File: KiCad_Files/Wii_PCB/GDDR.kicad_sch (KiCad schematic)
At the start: 2 parts

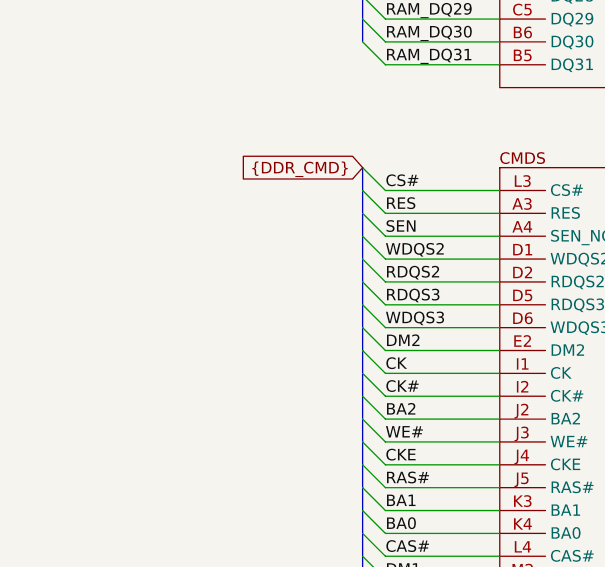
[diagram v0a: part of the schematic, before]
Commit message: Corrected C160 & RAM ZQ
C160 was updated from 4.7uF to 100nF.
RAM ZQ was grounded, it was working while floating, but updating anyway to ensure proper function.
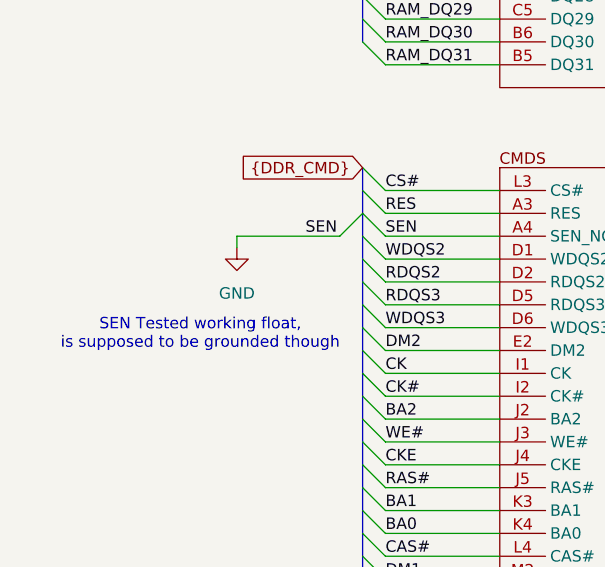
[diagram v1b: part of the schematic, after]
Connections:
- net SEN is gone; now on net GND: RAM1.A4 (SEN_NC)
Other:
- note added: "SEN Tested working float, is supposed to be grounded though"
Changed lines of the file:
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@@
 	(generator_version "9.0")
 	(paper "A4")
+	(text "SEN Tested working float,\nis supposed to be grounded though"
+		(exclude_from_sim no)
+		(at 27.686 145.542 0)
+		(effects
+			(font
+				(size 1.27 1.27)
+			)
+		)
+	)
 	(junction
 		(at 254 109.22)
@@
 	(bus_entry
 		(at 45.72 132.08)
+		(size -2.54 2.54)
+		(stroke
+			(width 0)
+			(type default)
+		)
+	)
+	(bus_entry
+		(at 45.72 132.08)
 		(size 2.54 2.54)
 		(stroke
@@
 	(wire
 		(pts
+			(xy 31.75 134.62) (xy 43.18 134.62)
+		)
+		(stroke
+			(width 0)
+			(type default)
+		)
+	)
+	(wire
+		(pts
 			(xy 254 116.84) (xy 243.84 116.84)
 		)
@@
 	(wire
 		(pts
+			(xy 31.75 134.62) (xy 31.75 135.89)
+		)
+		(stroke
+			(width 0)
+			(type default)
+		)
+	)
+	(wire
+		(pts
 			(xy 205.74 80.01) (xy 205.74 82.55)
 		)
@@
 		)
 	)
+	(label "SEN"
+		(at 39.37 134.62 0)
+		(effects
+			(font
+				(size 1.27 1.27)
+			)
+			(justify left bottom)
+		)
+	)
 	(label "RAM_A3"
 		(at 92.71 44.45 0)
@@
 	)
 	(symbol
-		(lib_name "Updated_GDDR3_1")
+		(lib_id "power:GND")
+		(at 31.75 135.89 0)
+		(unit 1)
+		(exclude_from_sim no)
+		(in_bom yes)
+		(on_board yes)
+		(dnp no)
+		(fields_autoplaced yes)
+		(property "Reference" "#PWR016"
+			(at 31.75 142.24 0)
+			(effects
+				(font
+					(size 1.27 1.27)
+				)
+				(hide yes)
+			)
+		)
+		(property "Value" "GND"
+			(at 31.75 140.97 0)
+			(effects
+				(font
+					(size 1.27 1.27)
+				)
+			)
+		)
+		(property "Footprint" ""
+			(at 31.75 135.89 0)
+			(effects
+				(font
+					(size 1.27 1.27)
+				)
+				(hide yes)
+			)
+		)
+		(property "Datasheet" ""
+			(at 31.75 135.89 0)
+			(effects
+				(font
+					(size 1.27 1.27)
+				)
+				(hide yes)
+			)
+		)
+		(property "Description" "Power symbol creates a global label with name \"GND\" , ground"
+			(at 31.75 135.89 0)
+			(effects
+				(font
+					(size 1.27 1.27)
+				)
+				(hide yes)
+			)
+		)
+		(pin "1"
+		)
+		(instances
+			(project "Wii PCB"
+				(path "/07becb85-5b32-497c-802d-66c73e9db46a/2c30263e-9c9a-4ac3-91af-18e443e3dbbc"
+					(reference "#PWR016")
+					(unit 1)
+				)
+			)
+		)
+	)
+	(symbol
 		(lib_id "Wii_symbols:Updated_GDDR3")
 		(at 74.93 29.21 0)

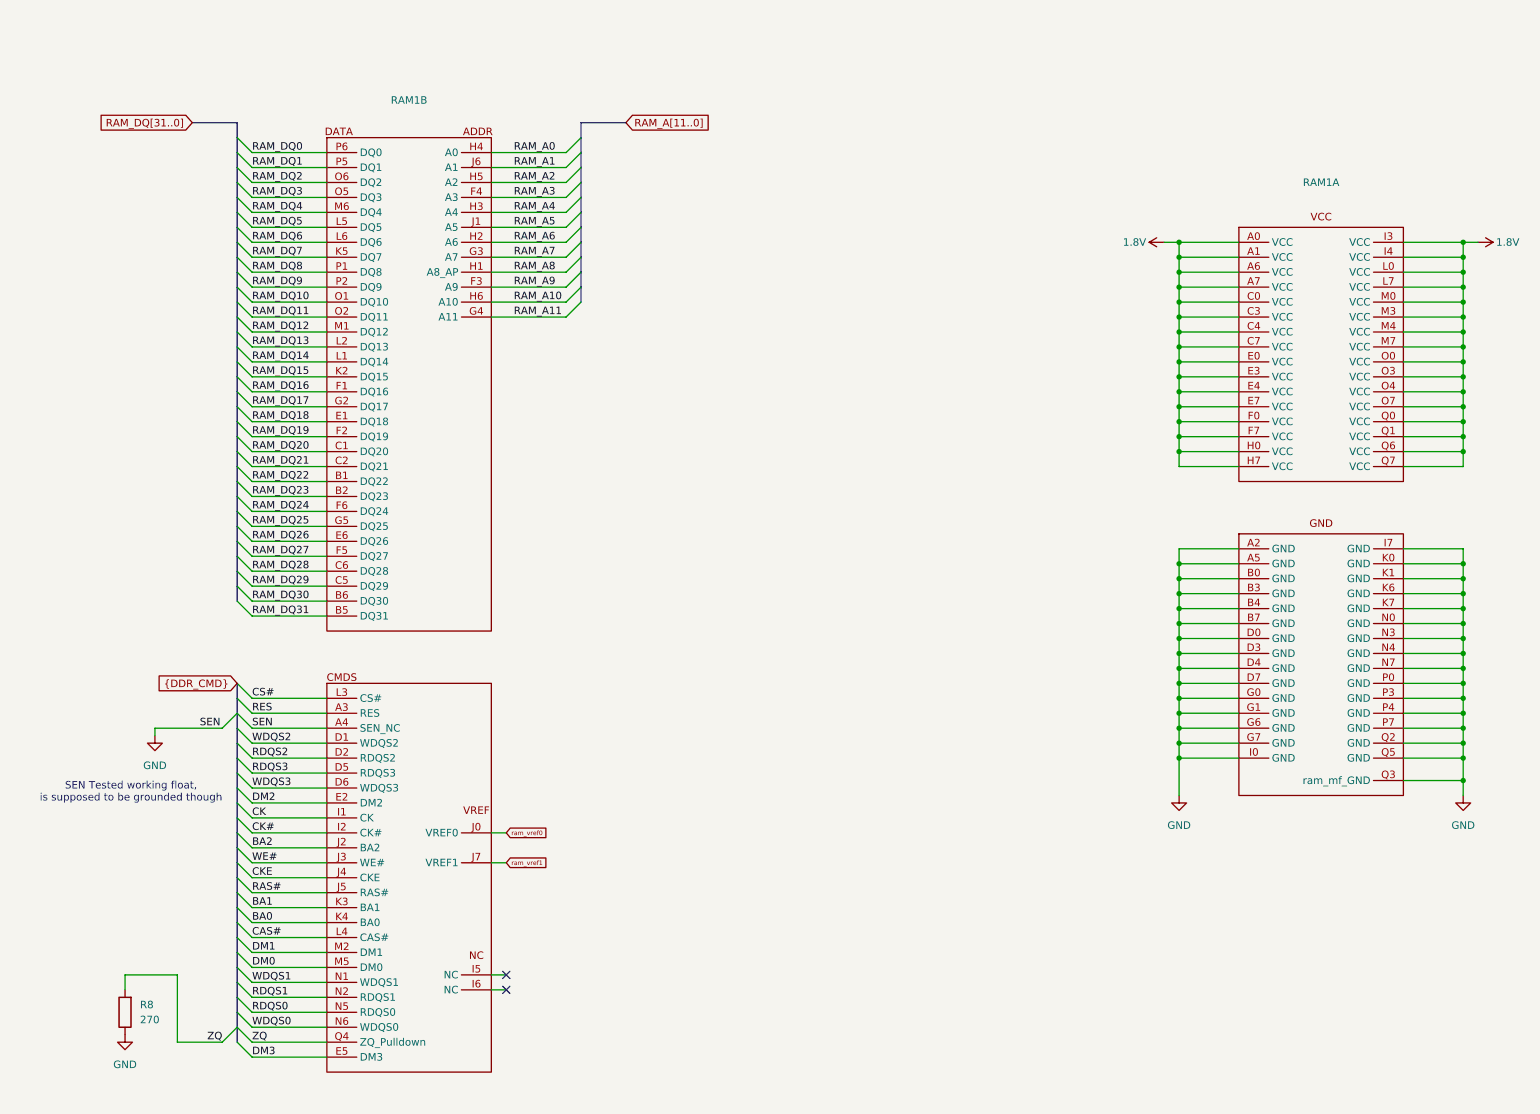
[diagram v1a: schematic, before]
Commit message: Updated RAM & GPU bus to allow custom net rules for measuring intra-track spacing, added pad for reset, removed debug pads, reorganized ram schematic to cluster length matched signals, changed MX chip and U10 symbols, and re-labeled the wifi net interface.
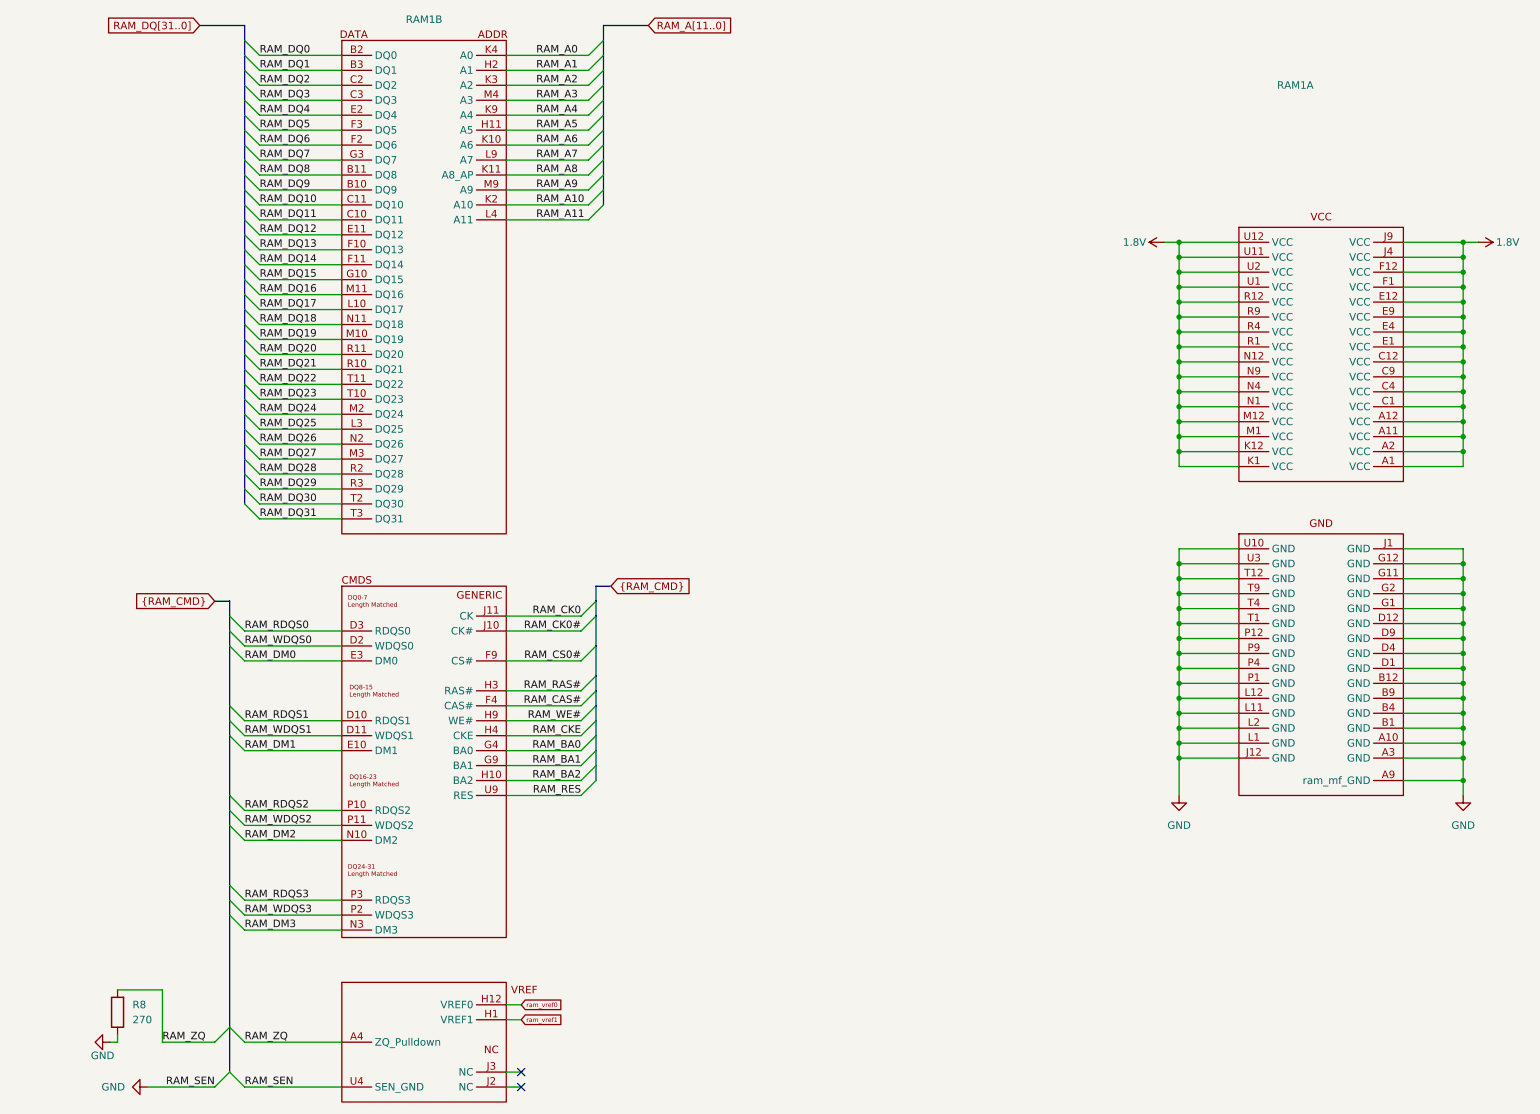
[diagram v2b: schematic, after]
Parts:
- removed RAM1: ~, wii_bgaLibrary:GDDR3, symbol Wii_symbols:Updated_GDDR3
- added RAM1: ~, WeeWii_Library:Updated GDDR3, symbol Wii_symbols:New_Updated_GDDR3
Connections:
- net 1.8V: now also RAM1.A1 (VCC), RAM1.A11 (VCC), RAM1.A12 (VCC), RAM1.A2 (VCC), RAM1.C1 (VCC), RAM1.C12 (VCC), RAM1.C4 (VCC), RAM1.C9 (VCC), RAM1.E1 (VCC), RAM1.E12 (VCC), RAM1.E4 (VCC), RAM1.E9 (VCC), RAM1.F1 (VCC), RAM1.F12 (VCC), RAM1.J4 (VCC), RAM1.J9 (VCC), RAM1.K1 (VCC), RAM1.K12 (VCC), RAM1.M1 (VCC), RAM1.M12 (VCC), RAM1.N1 (VCC), RAM1.N12 (VCC), RAM1.N4 (VCC), RAM1.N9 (VCC), RAM1.R1 (VCC), RAM1.R12 (VCC), RAM1.R4 (VCC), RAM1.R9 (VCC), RAM1.U1 (VCC), RAM1.U11 (VCC), RAM1.U12 (VCC), RAM1.U2 (VCC)
- net GND: now also RAM1.A10 (GND), RAM1.A3 (GND), RAM1.A9 (ram_mf_GND), RAM1.B1 (GND), RAM1.B12 (GND), RAM1.B4 (GND), RAM1.B9 (GND), RAM1.D1 (GND), RAM1.D12 (GND), RAM1.D4 (GND), RAM1.D9 (GND), RAM1.G1 (GND), RAM1.G11 (GND), RAM1.G12 (GND), RAM1.G2 (GND), RAM1.J1 (GND), RAM1.J12 (GND), RAM1.L1 (GND), RAM1.L11 (GND), RAM1.L12 (GND), RAM1.L2 (GND), RAM1.P1 (GND), RAM1.P12 (GND), RAM1.P4 (GND), RAM1.P9 (GND), RAM1.T1 (GND), RAM1.T12 (GND), RAM1.T4 (GND), RAM1.T9 (GND), RAM1.U10 (GND), RAM1.U3 (GND), RAM1.U4 (SEN_GND)
- net RAM_A0: now also RAM1.K4 (A0)
- net RAM_A1: now also RAM1.H2 (A1)
- net RAM_A10: now also RAM1.K2 (A10)
- net RAM_A11: now also RAM1.L4 (A11)
- net RAM_A2: now also RAM1.K3 (A2)
- net RAM_A3: now also RAM1.M4 (A3)
- net RAM_A4: now also RAM1.K9 (A4)
- net RAM_A5: now also RAM1.H11 (A5)
- net RAM_A6: now also RAM1.K10 (A6)
- net RAM_A7: now also RAM1.L9 (A7)
- net RAM_A8: now also RAM1.K11 (A8_AP)
- net RAM_A9: now also RAM1.M9 (A9)
- net RAM_DQ0: now also RAM1.B2 (DQ0)
- net RAM_DQ1: now also RAM1.B3 (DQ1)
- net RAM_DQ10: now also RAM1.C11 (DQ10)
- net RAM_DQ11: now also RAM1.C10 (DQ11)
- net RAM_DQ12: now also RAM1.E11 (DQ12)
- net RAM_DQ13: now also RAM1.F10 (DQ13)
- net RAM_DQ14: now also RAM1.F11 (DQ14)
- net RAM_DQ15: now also RAM1.G10 (DQ15)
- net RAM_DQ16: now also RAM1.M11 (DQ16)
- net RAM_DQ17: now also RAM1.L10 (DQ17)
- net RAM_DQ18: now also RAM1.N11 (DQ18)
- net RAM_DQ19: now also RAM1.M10 (DQ19)
- net RAM_DQ2: now also RAM1.C2 (DQ2)
- net RAM_DQ20: now also RAM1.R11 (DQ20)
- net RAM_DQ21: now also RAM1.R10 (DQ21)
- net RAM_DQ22: now also RAM1.T11 (DQ22)
- net RAM_DQ23: now also RAM1.T10 (DQ23)
- net RAM_DQ24: now also RAM1.M2 (DQ24)
- net RAM_DQ25: now also RAM1.L3 (DQ25)
- net RAM_DQ26: now also RAM1.N2 (DQ26)
- net RAM_DQ27: now also RAM1.M3 (DQ27)
- net RAM_DQ28: now also RAM1.R2 (DQ28)
- net RAM_DQ29: now also RAM1.R3 (DQ29)
- net RAM_DQ3: now also RAM1.C3 (DQ3)
- net RAM_DQ30: now also RAM1.T2 (DQ30)
- net RAM_DQ31: now also RAM1.T3 (DQ31)
- net RAM_DQ4: now also RAM1.E2 (DQ4)
- net RAM_DQ5: now also RAM1.F3 (DQ5)
- net RAM_DQ6: now also RAM1.F2 (DQ6)
- net RAM_DQ7: now also RAM1.G3 (DQ7)
- net RAM_DQ8: now also RAM1.B11 (DQ8)
- net RAM_DQ9: now also RAM1.B10 (DQ9)
- net ram_vref0: now also RAM1.H12 (VREF0)
- net ram_vref1: now also RAM1.H1 (VREF1)
- net ZQ renamed RAM_ZQ
- net RAM_ZQ: now also RAM1.A4 (ZQ_Pulldown)
- new net RAM_BA0: RAM1.G4 (BA0)
- new net RAM_BA1: RAM1.G9 (BA1)
- new net RAM_BA2: RAM1.H10 (BA2)
- new net RAM_CAS#: RAM1.F4 (CAS#)
- new net RAM_CK0: RAM1.J11 (CK)
- new net RAM_CK0#: RAM1.J10 (CK#)
- new net RAM_CKE: RAM1.H4 (CKE)
- new net RAM_CS0#: RAM1.F9 (CS#)
- new net RAM_DM0: RAM1.E3 (DM0)
- new net RAM_DM1: RAM1.E10 (DM1)
- new net RAM_DM2: RAM1.N10 (DM2)
- new net RAM_DM3: RAM1.N3 (DM3)
- new net RAM_RAS#: RAM1.H3 (RAS#)
- new net RAM_RDQS0: RAM1.D3 (RDQS0)
- new net RAM_RDQS1: RAM1.D10 (RDQS1)
- new net RAM_RDQS2: RAM1.P10 (RDQS2)
- new net RAM_RDQS3: RAM1.P3 (RDQS3)
- new net RAM_RES: RAM1.U9 (RES)
- new net RAM_WDQS0: RAM1.D2 (WDQS0)
- new net RAM_WDQS1: RAM1.D11 (WDQS1)
- new net RAM_WDQS2: RAM1.P11 (WDQS2)
- new net RAM_WDQS3: RAM1.P2 (WDQS3)
- new net RAM_WE#: RAM1.H9 (WE#)
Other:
- note removed: "SEN Tested working float, is supposed to be grounded though"
- moved on the sheet: R8
